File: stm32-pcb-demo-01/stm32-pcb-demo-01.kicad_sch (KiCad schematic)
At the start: 1 part, among them U1 STM32F405RGTx

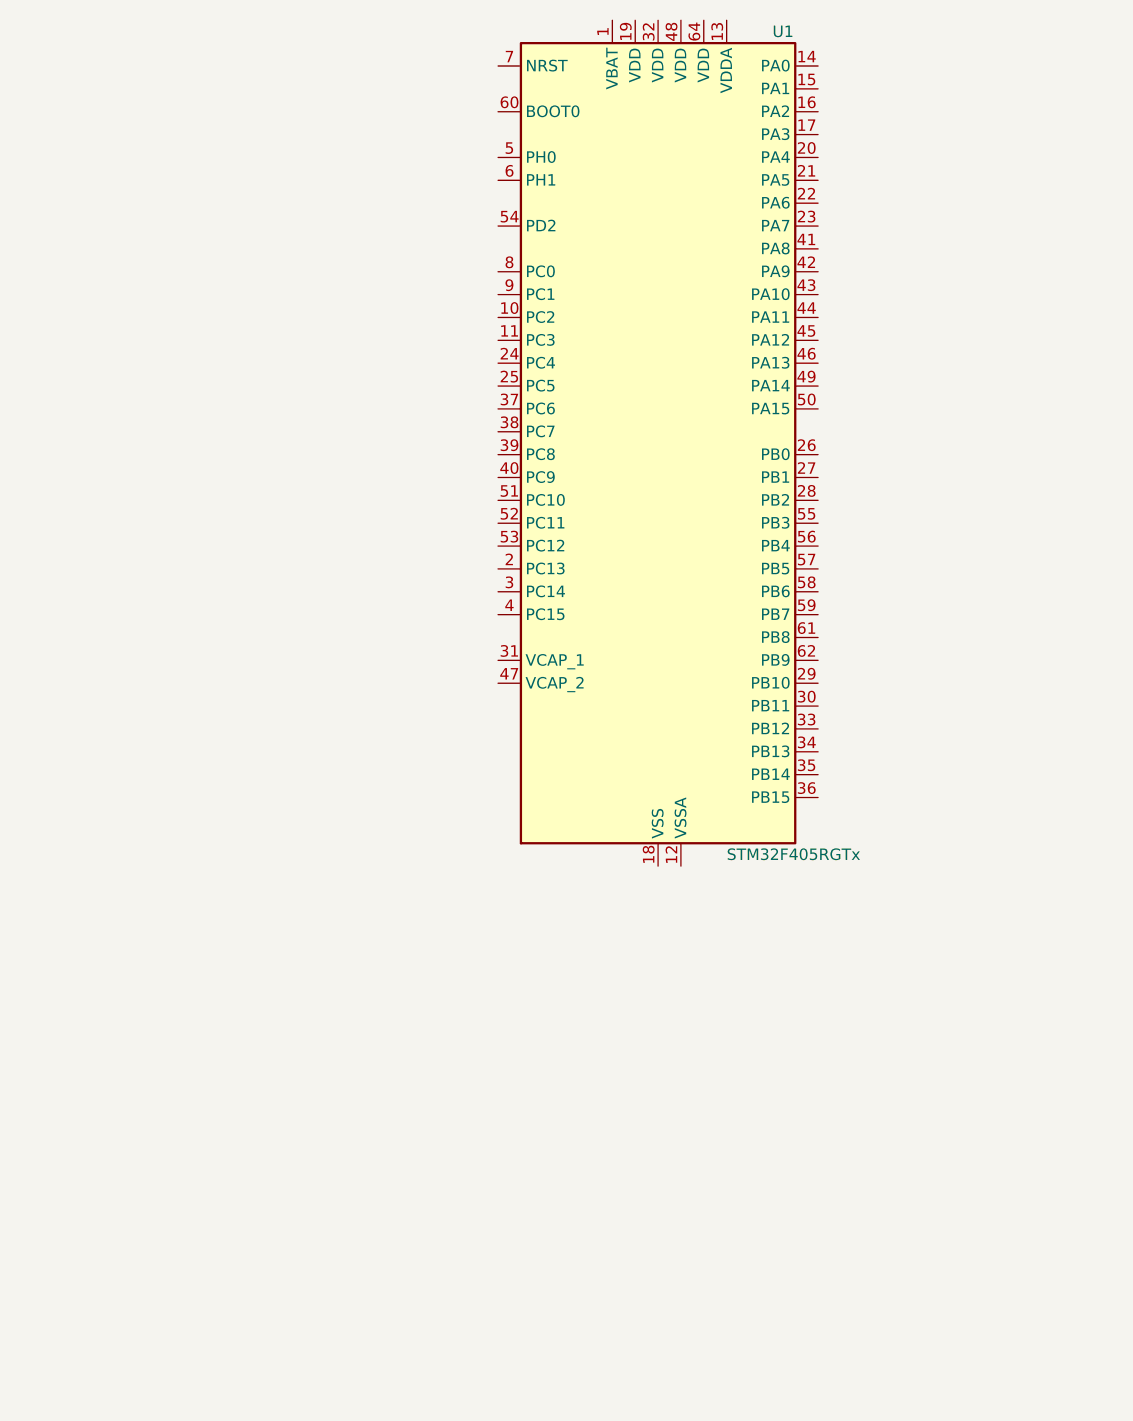
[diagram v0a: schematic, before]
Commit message: finish preliminary STM32 microcontroller circuitry
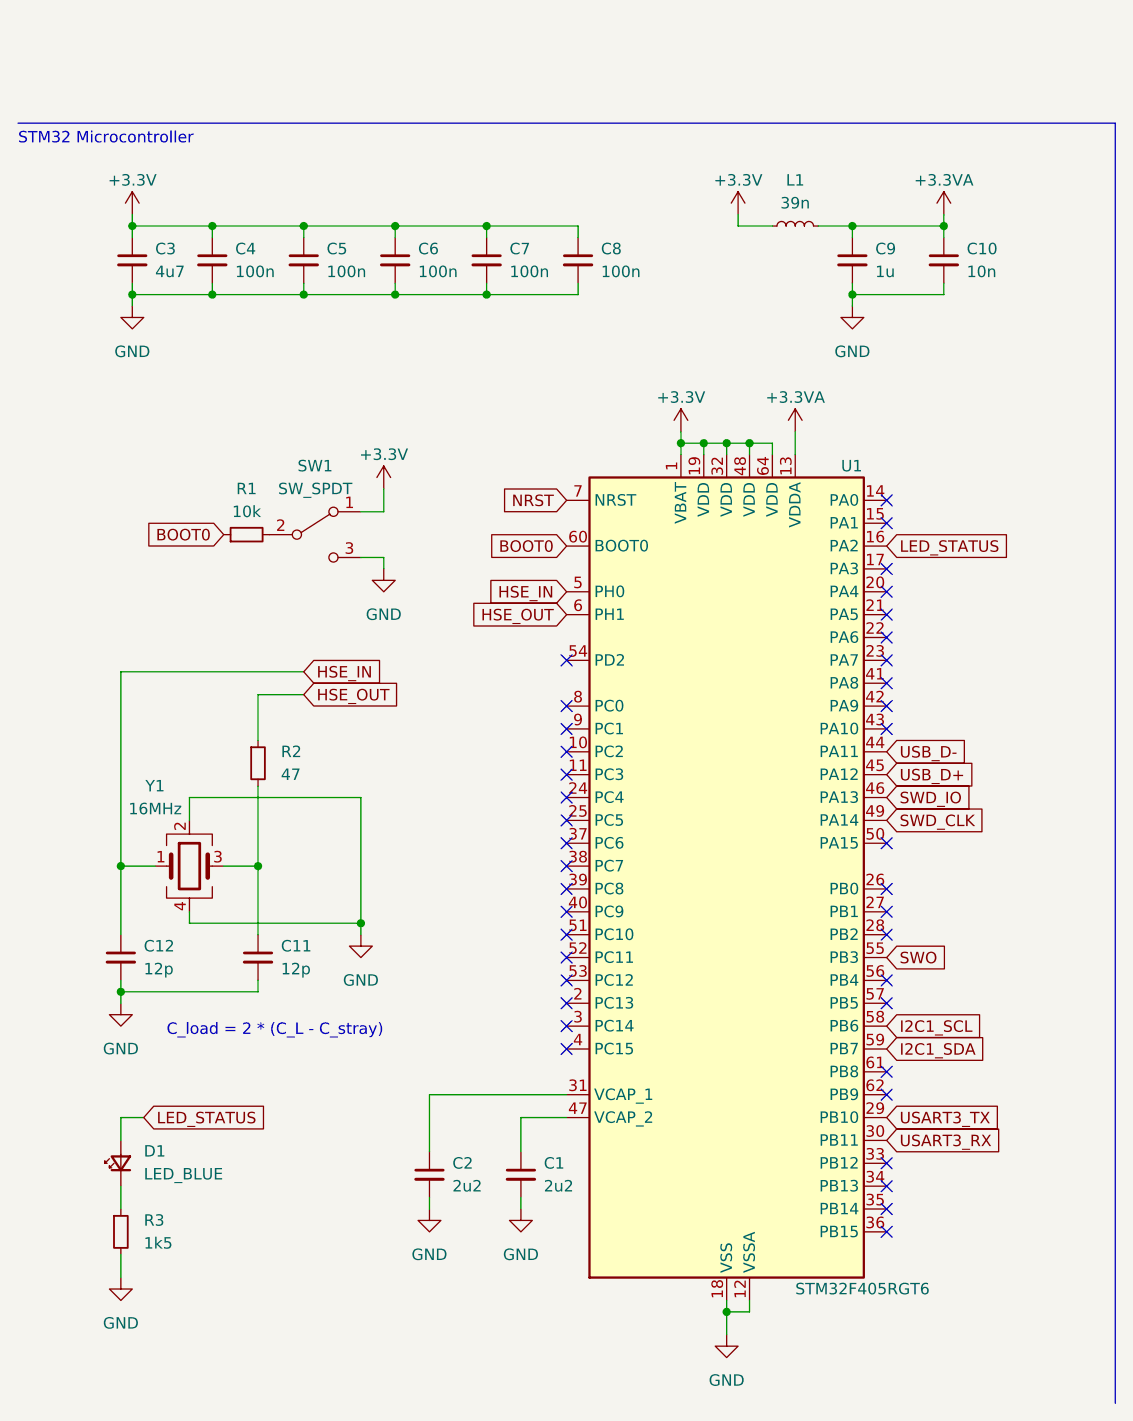
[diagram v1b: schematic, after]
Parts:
- added C1, C2: 2u2, symbol Device:C_Small
- added C10: 10n, symbol Device:C_Small
- added C11, C12: 12p, symbol Device:C_Small
- added C3: 4u7, symbol Device:C_Small
- added C4, C5, C6, C7, C8: 100n, symbol Device:C_Small
- added C9: 1u, symbol Device:C_Small
- added D1: LED_BLUE, symbol Device:LED_Small
- added L1: 39n, symbol Device:L_Small
- added R1: 10k, symbol Device:R_Small
- added R2: 47, symbol Device:R_Small
- added R3: 1k5, symbol Device:R_Small
- added SW1: SW_SPDT, symbol Switch:SW_SPDT
- added Y1: 16MHz, symbol Device:Crystal_GND24
- U1: value STM32F405RGTx -> STM32F405RGT6
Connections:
- net +3.3V: now reaches U1.1 (VBAT)
- net +3.3V: now also U1.19 (VDD), U1.32 (VDD), U1.48 (VDD), U1.64 (VDD), C3.1, C4.1, C5.1, C6.1, C7.1, C8.1, L1.1, SW1.1 (A)
- net GND: now reaches U1.12 (VSSA)
- net GND: now also U1.18 (VSS), U1.63 (VSS), C1.2, C10.2, C11.2, C12.2, C2.2, C3.2, C4.2, C5.2, C6.2, C7.2, C8.2, C9.2, R3.2, SW1.3 (C), Y1.2, Y1.4
- net +3.3VA: now reaches U1.13 (VDDA)
- net +3.3VA: now also C10.1, C9.1, L1.2
- net LED_STATUS: now reaches U1.16 (PA2)
- net LED_STATUS: now also D1.2 (A)
- net USART3_TX: now reaches U1.29 (PB10)
- net USART3_RX: now reaches U1.30 (PB11)
- net at U1.31 (VCAP_1): now also C2.1
- net USB_D-: now reaches U1.44 (PA11)
- net USB_D+: now reaches U1.45 (PA12)
- net SWD_IO: now reaches U1.46 (PA13)
- net at U1.47 (VCAP_2): now also C1.1
- net SWD_CLK: now reaches U1.49 (PA14)
- net HSE_IN: now reaches U1.5 (PH0)
- net HSE_IN: now also C12.1, Y1.1
- net SWO: now reaches U1.55 (PB3)
- net I2C1_SCL: now reaches U1.58 (PB6)
- net I2C1_SDA: now reaches U1.59 (PB7)
- net HSE_OUT: now reaches U1.6 (PH1)
- net HSE_OUT: now also R2.1
- net BOOT0: now reaches U1.60 (BOOT0)
- net BOOT0: now also R1.1
- net NRST: now reaches U1.7 (NRST)
- new net: D1.1 (K), R3.1
- new net: R1.2, SW1.2 (B)
- new net: C11.1, R2.2, Y1.3
- no-connect marks 0 -> 39
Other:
- note added: "C_load = 2 * (C_L - C_stray)"
- note added: "STM32 Microcontroller"
- moved on the sheet: U1
